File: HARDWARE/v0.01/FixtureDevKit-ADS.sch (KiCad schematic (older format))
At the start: 41 parts

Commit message: editing some files. cleaning stuff up.
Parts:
- removed J? (x5): Conn_01x04, symbol Conn_01x04
- removed R? (x32): 1K, symbol R
- removed U? (x4): ADS1015IDGST, symbol ADS1015IDGST
- added J? (x4): ADS 0, symbol Conn_01x04
- added J? (x10): ADS0, symbol Conn_01x04
- added R? (x32): 1K, symbol R
- added U? (x4): ADS1015IDGST, symbol ADS1015IDGST
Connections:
- net GND: now also J?.3 (Pin_3), J?.3 (Pin_3), J?.3 (Pin_3), J?.3 (Pin_3), J?.3 (Pin_3), J?.3 (Pin_3), J?.3 (Pin_3), J?.3 (Pin_3), J?.3 (Pin_3), J?.3 (Pin_3), R?.1, R?.1, R?.1, R?.1, R?.1, R?.1, R?.1, R?.1, R?.1, R?.1, R?.1, R?.1, R?.1, R?.1, R?.1, R?.1, U?.1 (ADDR), U?.3 (GND), U?.3 (GND), U?.3 (GND), U?.3 (GND)
- new net: R?.2, U?.4 (AIN0) (x4)
- new net: R?.2, U?.5 (AIN1) (x4)
- new net: R?.2, U?.6 (AIN2) (x4)
- new net: R?.2, U?.7 (AIN3) (x4)
- new net: J?.1 (Pin_1), R?.1, R?.2 (x4)
- new net: J?.2 (Pin_2), R?.1, R?.2 (x4)
- new net: J?.3 (Pin_3), R?.1, R?.2 (x4)
- new net: J?.4 (Pin_4), R?.1, R?.2 (x4)
- new net SCL: J?.1 (Pin_1), J?.1 (Pin_1), J?.1 (Pin_1), J?.1 (Pin_1), J?.1 (Pin_1), J?.1 (Pin_1), J?.1 (Pin_1), J?.1 (Pin_1), J?.1 (Pin_1), J?.1 (Pin_1), U?.1 (ADDR), U?.10 (SCL), U?.10 (SCL), U?.10 (SCL), U?.10 (SCL)
- new net SDA: J?.2 (Pin_2), J?.2 (Pin_2), J?.2 (Pin_2), J?.2 (Pin_2), J?.2 (Pin_2), J?.2 (Pin_2), J?.2 (Pin_2), J?.2 (Pin_2), J?.2 (Pin_2), J?.2 (Pin_2), U?.1 (ADDR), U?.9 (SDA), U?.9 (SDA), U?.9 (SDA), U?.9 (SDA)
- new net VS: J?.4 (Pin_4), J?.4 (Pin_4), J?.4 (Pin_4), J?.4 (Pin_4), J?.4 (Pin_4), J?.4 (Pin_4), J?.4 (Pin_4), J?.4 (Pin_4), J?.4 (Pin_4), J?.4 (Pin_4), U?.1 (ADDR), U?.8 (VDD), U?.8 (VDD), U?.8 (VDD), U?.8 (VDD)
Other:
- note added: "ADS_0\n"
- note added: "ADS_1"
- note added: "ADS_2"
- note added: "ADS_3"
- note added: "AIN0"
- note added: "AIN1"
- note added: "AIN2"
- note added: "AIN3"
- note added: "I2C addr 0x49"
- note added: "I2C addr 0x4A"
- note added: "Main Circuit\nHeaders"
- note removed: "GND\n"
- note removed: "I2C addr 0x49\n"
- note removed: "I2C addr 0x4A\n"
- note removed: "NC"
- note removed: "SCL"
- note removed: "SDA"
- note removed: "TO DO:\n- verify I2C addresses\n- verify voltage devider methodology"
- note removed: "VCC"
- note removed: "VCC-IN-0"
- note removed: "VCC-IN-1"
- note removed: "VCC-IN-2\n"
- note removed: "VCC-IN-3"

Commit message: o gosh
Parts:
- added C? (x4): 0.1uF, symbol C
- J?: value ADS 0 -> ADS1
- J? (x2): value ADS0 -> ADS1
- J? (x2): value ADS 0 -> ADS3
- J?: value ADS0 -> ADS2
- J? (x3): value ADS0 -> ADS3
- J? (x2): value ADS0 -> ADS
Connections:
- net GND: now also C?.2, C?.2, C?.2, C?.2
- net VS: now also C?.1, C?.1, C?.1, C?.1
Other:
- note added: "TO DO:\n- is it okay to have so many headers on the I2C lines?\n- Do we want the cut trace connector or not connect?\n- where do we want to add test points?\n- power-supply decoupling capacitor to GND. 0.1uF"
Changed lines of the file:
@@
 Wire Wire Line
 	800  2400 900  2400
-Text Notes 1100 2850 0    60   ~ 0
+Text Notes 3100 1400 0    60   ~ 0
 I2C addr 0x48\n
 Wire Wire Line
@@
 P 6600 2300
 F 0 "J?" H 6600 2500 50  0000 C CNN
-F 1 "ADS 0" H 6600 2000 50  0000 C CNN
+F 1 "ADS1" H 6600 2000 50  0000 C CNN
 F 2 "" H 6600 2300 50  0001 C CNN
 F 3 "" H 6600 2300 50  0001 C CNN
@@
 Wire Wire Line
 	5250 2600 5250 2650
-Text Notes 4350 2850 0    60   ~ 0
+Text Notes 6350 1400 0    60   ~ 0
 I2C addr 0x49
 Wire Wire Line
@@
 P 4700 1450
 F 0 "J?" H 4700 1650 50  0000 C CNN
-F 1 "ADS0" H 4700 1150 50  0000 C CNN
+F 1 "ADS1" H 4700 1150 50  0000 C CNN
 F 2 "" H 4700 1450 50  0001 C CNN
 F 3 "" H 4700 1450 50  0001 C CNN
@@
 P 4700 3500
 F 0 "J?" H 4700 3700 50  0000 C CNN
-F 1 "ADS0" H 4700 3200 50  0000 C CNN
+F 1 "ADS1" H 4700 3200 50  0000 C CNN
 F 2 "" H 4700 3500 50  0001 C CNN
 F 3 "" H 4700 3500 50  0001 C CNN
@@
 P 3350 5000
 F 0 "J?" H 3350 5200 50  0000 C CNN
-F 1 "ADS 0" H 3350 4700 50  0000 C CNN
+F 1 "ADS3" H 3350 4700 50  0000 C CNN
 F 2 "" H 3350 5000 50  0001 C CNN
 F 3 "" H 3350 5000 50  0001 C CNN
@@
 Wire Wire Line
 	2000 5300 2000 5350
-Text Notes 1100 5550 0    60   ~ 0
+Text Notes 3100 4100 0    60   ~ 0
 I2C addr 0x4A
 Wire Wire Line
@@
 P 1450 4150
 F 0 "J?" H 1450 4350 50  0000 C CNN
-F 1 "ADS0" H 1450 3850 50  0000 C CNN
+F 1 "ADS2" H 1450 3850 50  0000 C CNN
 F 2 "" H 1450 4150 50  0001 C CNN
 F 3 "" H 1450 4150 50  0001 C CNN
@@
 P 1450 6200
 F 0 "J?" H 1450 6400 50  0000 C CNN
-F 1 "ADS0" H 1450 5900 50  0000 C CNN
+F 1 "ADS3" H 1450 5900 50  0000 C CNN
 F 2 "" H 1450 6200 50  0001 C CNN
 F 3 "" H 1450 6200 50  0001 C CNN
@@
 P 6600 5000
 F 0 "J?" H 6600 5200 50  0000 C CNN
-F 1 "ADS 0" H 6600 4700 50  0000 C CNN
+F 1 "ADS3" H 6600 4700 50  0000 C CNN
 F 2 "" H 6600 5000 50  0001 C CNN
 F 3 "" H 6600 5000 50  0001 C CNN
@@
 Wire Wire Line
 	5250 5300 5250 5350
-Text Notes 4350 5550 0    60   ~ 0
+Text Notes 6350 4100 0    60   ~ 0
 I2C addr 0x4B
 Wire Wire Line
@@
 P 4700 4150
 F 0 "J?" H 4700 4350 50  0000 C CNN
-F 1 "ADS0" H 4700 3850 50  0000 C CNN
+F 1 "ADS3" H 4700 3850 50  0000 C CNN
 F 2 "" H 4700 4150 50  0001 C CNN
 F 3 "" H 4700 4150 50  0001 C CNN
@@
 P 4700 6200
 F 0 "J?" H 4700 6400 50  0000 C CNN
-F 1 "ADS0" H 4700 5900 50  0000 C CNN
+F 1 "ADS3" H 4700 5900 50  0000 C CNN
 F 2 "" H 4700 6200 50  0001 C CNN
 F 3 "" H 4700 6200 50  0001 C CNN
@@
 	4150 2600 4100 2600
 Wire Wire Line
-	4100 2600 4100 2400
+	4100 2400 4100 2650
 Wire Wire Line
 	4100 2400 4150 2400
@@
 P 7700 1700
 F 0 "J?" H 7700 1900 50  0000 C CNN
-F 1 "ADS0" H 7700 1400 50  0000 C CNN
+F 1 "ADS" H 7700 1400 50  0000 C CNN
 F 2 "" H 7700 1700 50  0001 C CNN
 F 3 "" H 7700 1700 50  0001 C CNN
@@
 P 7700 2450
 F 0 "J?" H 7700 2650 50  0000 C CNN
-F 1 "ADS0" H 7700 2150 50  0000 C CNN
+F 1 "ADS" H 7700 2150 50  0000 C CNN
 F 2 "" H 7700 2450 50  0001 C CNN
 F 3 "" H 7700 2450 50  0001 C CNN
@@
 Wire Notes Line
 	7100 1450 8650 1450
+Text Notes -7350 1450 0    157  ~ 0
+TO DO:\n- is it okay to have so many headers on the I2C lines?\n- Do we want the cut trace connector or not connect?\n- where do we want to add test points?\n- power-supply decoupling capacitor to GND. 0.1uF
+$Comp
+L C C?
+U 1 1 59EFF32D
+P 850 2800
+F 0 "C?" H 875 2900 50  0000 L CNN
+F 1 "0.1uF" H 875 2700 50  0000 L CNN
+F 2 "" H 888 2650 50  0001 C CNN
+F 3 "" H 850 2800 50  0001 C CNN
+	1    850  2800
+	1    0    0    -1
+$EndComp
+$Comp
+L GND #PWR?
+U 1 1 59EFF3E5
+P 850 3000
+F 0 "#PWR?" H 850 2750 50  0001 C CNN
+F 1 "GND" H 850 2850 50  0000 C CNN
+F 2 "" H 850 3000 50  0001 C CNN
+F 3 "" H 850 3000 50  0001 C CNN
+	1    850  3000
+	1    0    0    -1
+$EndComp
+Wire Wire Line
+	850  2600 850  2650
+Wire Wire Line
+	850  2950 850  3000
+$Comp
+L C C?
+U 1 1 59EFFF9A
+P 4100 2800
+F 0 "C?" H 4125 2900 50  0000 L CNN
+F 1 "0.1uF" H 4125 2700 50  0000 L CNN
+F 2 "" H 4138 2650 50  0001 C CNN
+F 3 "" H 4100 2800 50  0001 C CNN
+	1    4100 2800
+	1    0    0    -1
+$EndComp
+$Comp
+L GND #PWR?
+U 1 1 59F0004D
+P 4100 3000
+F 0 "#PWR?" H 4100 2750 50  0001 C CNN
+F 1 "GND" H 4100 2850 50  0000 C CNN
+F 2 "" H 4100 3000 50  0001 C CNN
+F 3 "" H 4100 3000 50  0001 C CNN
+	1    4100 3000
+	1    0    0    -1
+$EndComp
+Connection ~ 4100 2600
+Wire Wire Line
+	4100 2950 4100 3000
+$Comp
+L C C?
+U 1 1 59F0069D
+P 850 5500
+F 0 "C?" H 875 5600 50  0000 L CNN
+F 1 "0.1uF" H 875 5400 50  0000 L CNN
+F 2 "" H 888 5350 50  0001 C CNN
+F 3 "" H 850 5500 50  0001 C CNN
+	1    850  5500
+	1    0    0    -1
+$EndComp
+$Comp
+L GND #PWR?
+U 1 1 59F00AA9
+P 850 5700
+F 0 "#PWR?" H 850 5450 50  0001 C CNN
+F 1 "GND" H 850 5550 50  0000 C CNN
+F 2 "" H 850 5700 50  0001 C CNN
+F 3 "" H 850 5700 50  0001 C CNN
+	1    850  5700
+	1    0    0    -1
+$EndComp
+Wire Wire Line
+	850  5300 850  5350
+Wire Wire Line
+	850  5650 850  5700
+$Comp
+L C C?
+U 1 1 59F00D22
+P 4100 5500
+F 0 "C?" H 4125 5600 50  0000 L CNN
+F 1 "0.1uF" H 4125 5400 50  0000 L CNN
+F 2 "" H 4138 5350 50  0001 C CNN
+F 3 "" H 4100 5500 50  0001 C CNN
+	1    4100 5500
+	1    0    0    -1
+$EndComp
+$Comp
+L GND #PWR?
+U 1 1 59F00E3C
+P 4100 5700
+F 0 "#PWR?" H 4100 5450 50  0001 C CNN
+F 1 "GND" H 4100 5550 50  0000 C CNN
+F 2 "" H 4100 5700 50  0001 C CNN
+F 3 "" H 4100 5700 50  0001 C CNN
+	1    4100 5700
+	1    0    0    -1
+$EndComp
+Wire Wire Line
+	4100 5300 4100 5350
+Wire Wire Line
+	4100 5650 4100 5700
 $EndSCHEMATC

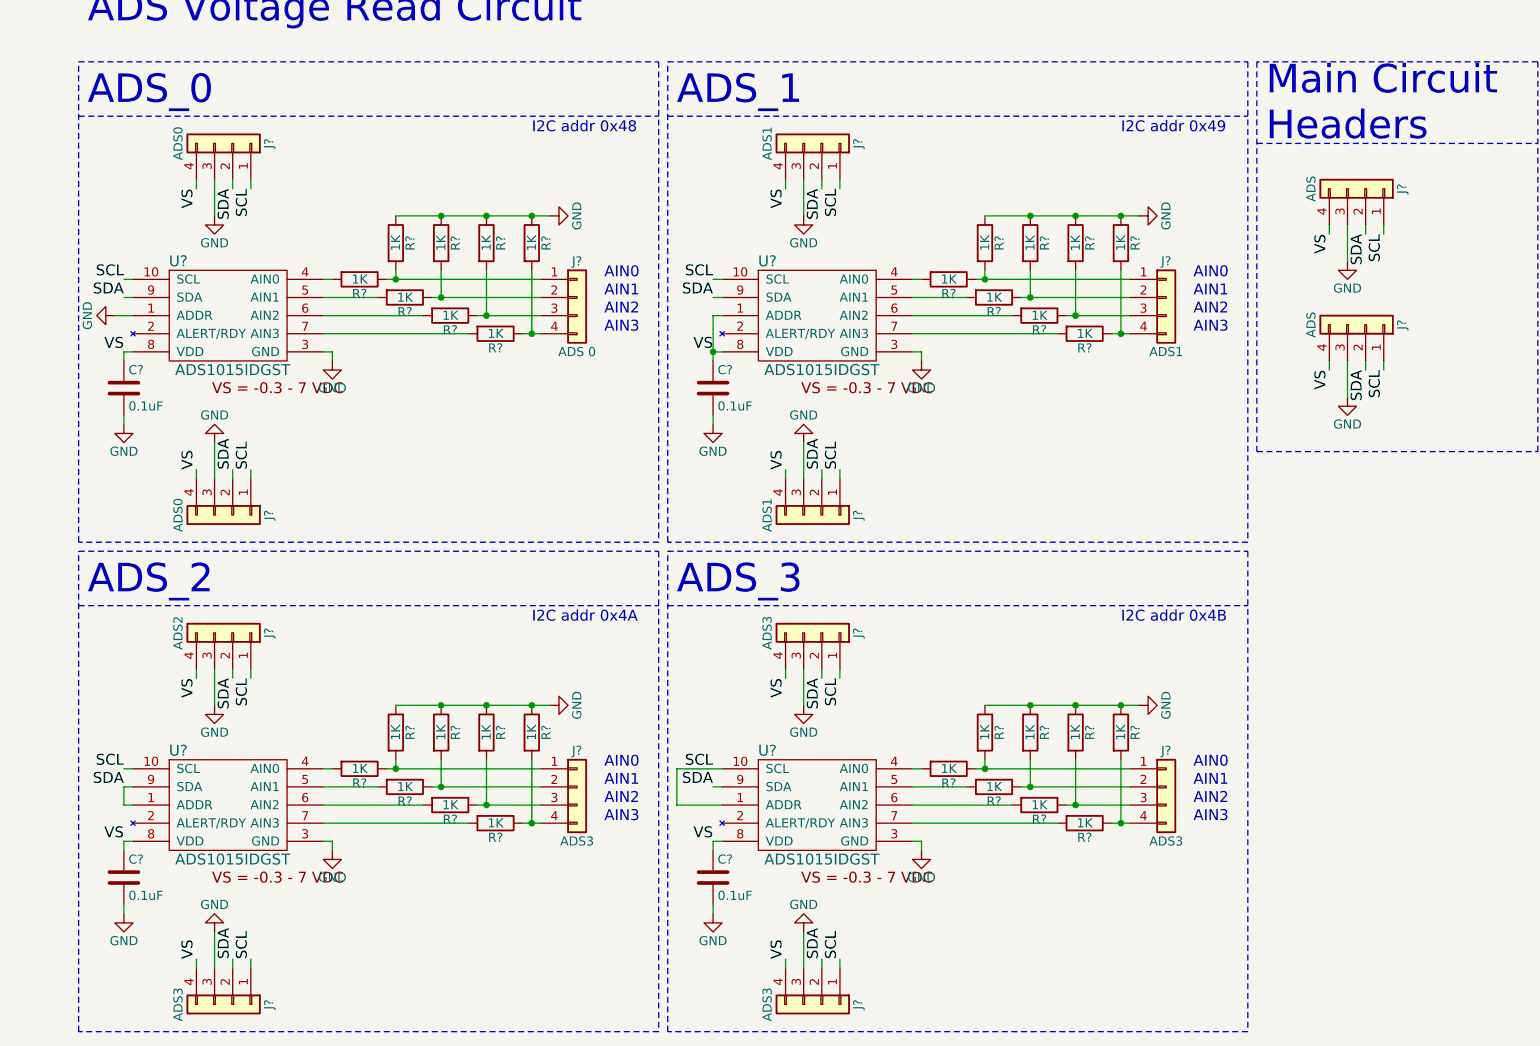
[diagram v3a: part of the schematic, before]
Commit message: adding netlist and design rules check
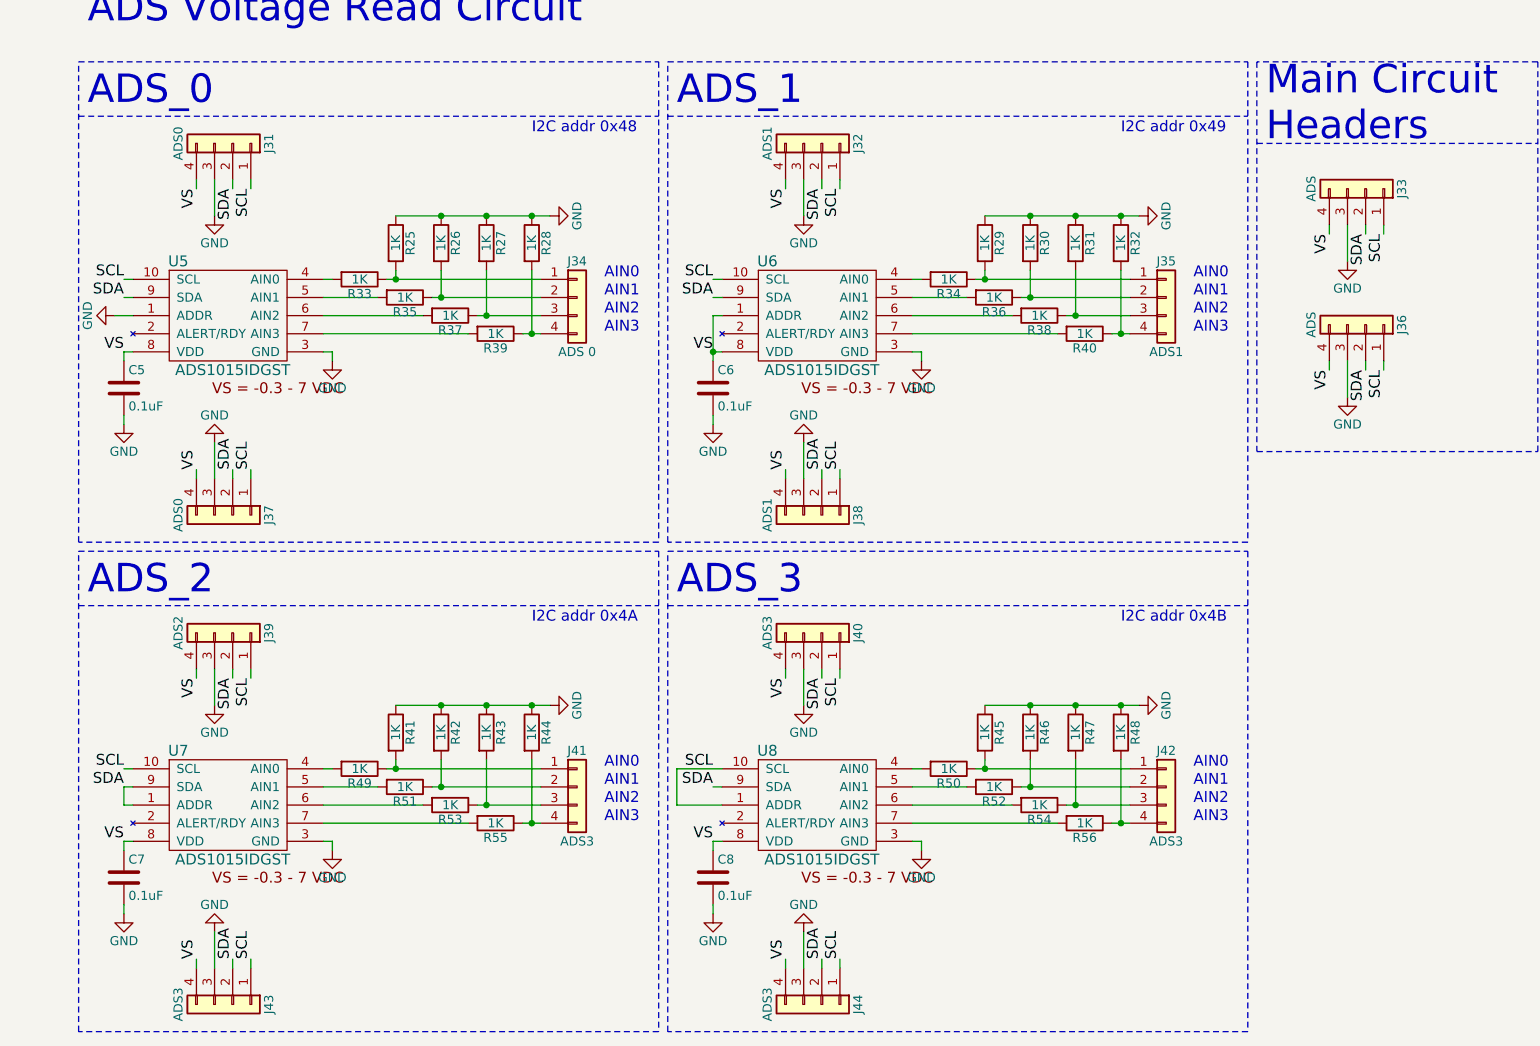
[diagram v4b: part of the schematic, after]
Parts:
- gave numbers to parts that had none: 54

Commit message: updating a few blocks, adding test points
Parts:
- J31: value ADS0 -> ADS_0
- J32: value ADS1 -> ADS_1
- J39: value ADS2 -> ADS_2
- J40: value ADS3 -> ADS_3
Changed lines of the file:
@@
 P 1450 1450
 F 0 "J31" H 1450 1650 50  0000 C CNN
-F 1 "ADS0" H 1450 1150 50  0000 C CNN
+F 1 "ADS_0" H 1450 1150 50  0000 C CNN
 F 2 "" H 1450 1450 50  0001 C CNN
 F 3 "" H 1450 1450 50  0001 C CNN
@@
 P 4700 1450
 F 0 "J32" H 4700 1650 50  0000 C CNN
-F 1 "ADS1" H 4700 1150 50  0000 C CNN
+F 1 "ADS_1" H 4700 1150 50  0000 C CNN
 F 2 "" H 4700 1450 50  0001 C CNN
 F 3 "" H 4700 1450 50  0001 C CNN
@@
 P 1450 4150
 F 0 "J39" H 1450 4350 50  0000 C CNN
-F 1 "ADS2" H 1450 3850 50  0000 C CNN
+F 1 "ADS_2" H 1450 3850 50  0000 C CNN
 F 2 "" H 1450 4150 50  0001 C CNN
 F 3 "" H 1450 4150 50  0001 C CNN
@@
 P 4700 4150
 F 0 "J40" H 4700 4350 50  0000 C CNN
-F 1 "ADS3" H 4700 3850 50  0000 C CNN
+F 1 "ADS_3" H 4700 3850 50  0000 C CNN
 F 2 "" H 4700 4150 50  0001 C CNN
 F 3 "" H 4700 4150 50  0001 C CNN
